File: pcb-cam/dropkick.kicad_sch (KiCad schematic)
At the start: 50 parts, among them J1 Conn_01x13, J2 3221-10-0300-00-TR, SW1 450405020524, SW2 KMR211NG_LFS, U1 SPX3819-3.3, U2 MCP73831T-2ACI/OT, U3 CAM-M8C-0, U4 ATSAMD21G18A-AUT, U5 DPS310XTSA1, U6 MPU-6050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

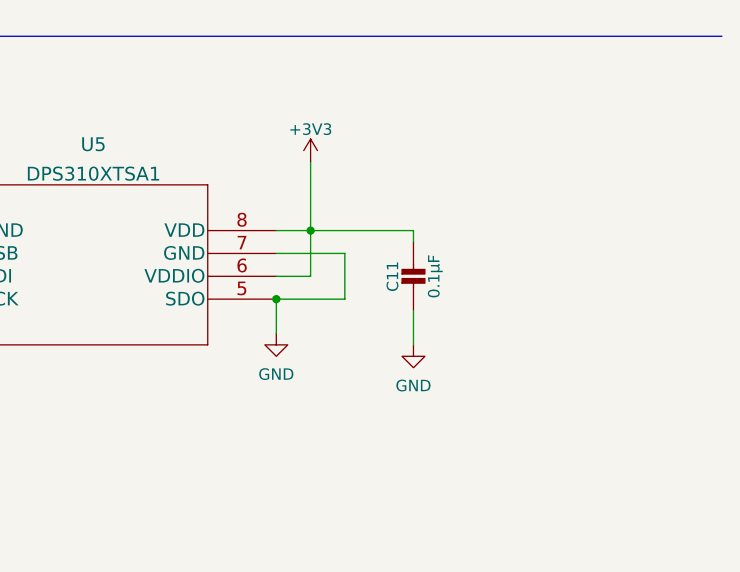
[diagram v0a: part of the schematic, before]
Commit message: Added extra CAP per DPS310 datasheet
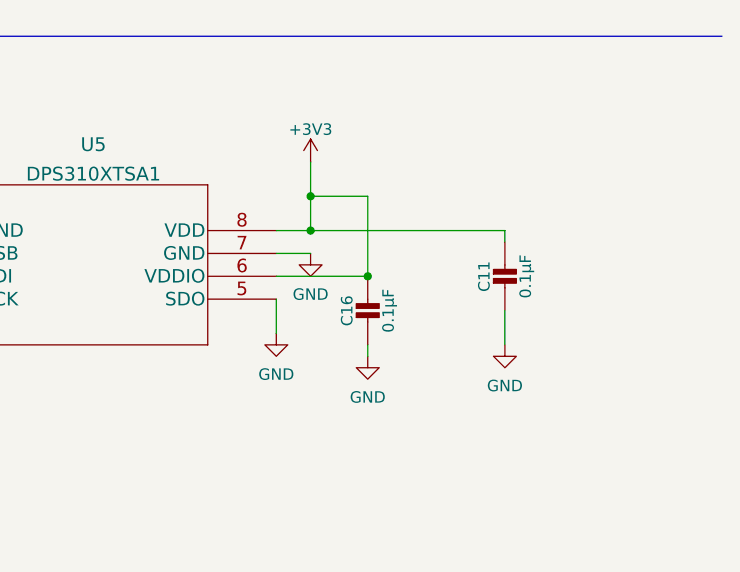
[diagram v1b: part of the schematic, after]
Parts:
- added C16: 0.1µF, Capacitor_SMD:C_0603_1608Metric, symbol Adafruit MPU6050-eagle-import:CAP_CERAMIC0603_NO
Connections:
- net +3V3: now also C16.1
- net GND: now also C16.2
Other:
- moved on the sheet: C11
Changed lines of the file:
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@@
   (junction (at 283.21 83.82) (diameter 0) (color 0 0 0 0)
   )
+  (junction (at 377.19 212.09) (diameter 0) (color 0 0 0 0)
+  )
   (junction (at 349.25 124.46) (diameter 0) (color 0 0 0 0)
   )
@@
   (junction (at 349.25 154.94) (diameter 0) (color 0 0 0 0)
   )
-  (junction (at 367.03 214.63) (diameter 0) (color 0 0 0 0)
-  )
   (junction (at 278.13 93.98) (diameter 0) (color 0 0 0 0)
   )
@@
   (junction (at 276.86 44.45) (diameter 0) (color 0 0 0 0)
   )
+  (junction (at 370.84 203.2) (diameter 0) (color 0 0 0 0)
+  )
   (junction (at 143.51 46.99) (diameter 0) (color 0 0 0 0)
   )
@@
     (stroke (width 0) (type default))
   )
-  (wire (pts (xy 370.84 207.01) (xy 382.27 207.01))
+  (wire (pts (xy 370.84 207.01) (xy 392.43 207.01))
     (stroke (width 0) (type default))
   )
@@
     (stroke (width 0) (type default))
   )
+  (wire (pts (xy 370.84 203.2) (xy 370.84 207.01))
+    (stroke (width 0) (type default))
+  )
   (wire (pts (xy 180.34 146.05) (xy 180.34 133.35))
     (stroke (width 0) (type default))
@@
     (stroke (width 0) (type default))
   )
-  (wire (pts (xy 382.27 215.9) (xy 382.27 219.71))
+  (wire (pts (xy 392.43 215.9) (xy 392.43 219.71))
     (stroke (width 0) (type default))
   )
@@
     (stroke (width 0) (type default))
   )
-  (wire (pts (xy 370.84 212.09) (xy 367.03 212.09))
-    (stroke (width 0) (type default))
-  )
   (wire (pts (xy 349.25 121.92) (xy 349.25 124.46))
     (stroke (width 0) (type default))
@@
     (stroke (width 0) (type default))
   )
-  (wire (pts (xy 382.27 207.01) (xy 382.27 208.28))
+  (wire (pts (xy 392.43 207.01) (xy 392.43 208.28))
     (stroke (width 0) (type default))
   )
@@
     (stroke (width 0) (type default))
   )
+  (wire (pts (xy 367.03 209.55) (xy 370.84 209.55))
+    (stroke (width 0) (type default))
+  )
   (wire (pts (xy 27.94 39.37) (xy 22.86 39.37))
     (stroke (width 0) (type default))
@@
     (stroke (width 0) (type default))
   )
-  (wire (pts (xy 374.65 214.63) (xy 367.03 214.63))
-    (stroke (width 0) (type default))
-  )
   (wire (pts (xy 100.33 52.07) (xy 100.33 57.15))
     (stroke (width 0) (type default))
@@
     (stroke (width 0) (type default))
   )
+  (wire (pts (xy 367.03 212.09) (xy 377.19 212.09))
+    (stroke (width 0) (type default))
+  )
   (wire (pts (xy 58.42 54.61) (xy 58.42 57.15))
     (stroke (width 0) (type default))
@@
     (stroke (width 0) (type default))
   )
-  (wire (pts (xy 374.65 209.55) (xy 374.65 214.63))
+  (wire (pts (xy 250.19 38.1) (xy 250.19 35.56))
     (stroke (width 0) (type default))
   )
-  (wire (pts (xy 250.19 38.1) (xy 250.19 35.56))
+  (wire (pts (xy 377.19 203.2) (xy 370.84 203.2))
     (stroke (width 0) (type default))
   )
@@
     (stroke (width 0) (type default))
   )
-  (wire (pts (xy 367.03 209.55) (xy 374.65 209.55))
+  (wire (pts (xy 377.19 219.71) (xy 377.19 220.98))
     (stroke (width 0) (type default))
   )
@@
     (stroke (width 0) (type default))
   )
+  (wire (pts (xy 377.19 212.09) (xy 377.19 203.2))
+    (stroke (width 0) (type default))
+  )
   (wire (pts (xy 78.74 212.09) (xy 78.74 214.63))
     (stroke (width 0) (type default))
@@
     (stroke (width 0) (type default))
   )
-  (wire (pts (xy 370.84 207.01) (xy 370.84 212.09))
-    (stroke (width 0) (type default))
-  )
   (wire (pts (xy 163.83 73.66) (xy 163.83 76.2))
     (stroke (width 0) (type default))
@@
     (stroke (width 0) (type default))
   )
-  (wire (pts (xy 370.84 199.39) (xy 370.84 207.01))
+  (wire (pts (xy 370.84 199.39) (xy 370.84 203.2))
     (stroke (width 0) (type default))
   )
@@
     )
   )
+  (symbol (lib_id "power:GND") (at 370.84 209.55 0) (unit 1)
+    (in_bom yes) (on_board yes) (dnp no) (fields_autoplaced)
+    (property "Reference" "#PWR08" (at 370.84 215.9 0)
+      (effects (font (size 1.27 1.27)) hide)
+    )
+    (property "Value" "GND" (at 370.84 214.1125 0)
+      (effects (font (size 1.27 1.27)))
+    )
+    (property "Footprint" "" (at 370.84 209.55 0)
+      (effects (font (size 1.27 1.27)) hide)
+    )
+    (property "Datasheet" "" (at 370.84 209.55 0)
+      (effects (font (size 1.27 1.27)) hide)
+    )
+    (pin "1")
+    (instances
+      (project "dropkick"
+        (path "/2b2dde1b-cbce-41fa-8b99-d2f668db6852"
+          (reference "#PWR08") (unit 1)
+        )
+      )
+    )
+  )
   (symbol (lib_id "Adafruit Feather M0 Adalogger-eagle-import:GND") (at 129.54 76.2 180) (unit 1)
     (in_bom yes) (on_board yes) (dnp no)
@@
     )
   )
+  (symbol (lib_id "power:GND") (at 377.19 220.98 0) (unit 1)
+    (in_bom yes) (on_board yes) (dnp no) (fields_autoplaced)
+    (property "Reference" "#PWR09" (at 377.19 227.33 0)
+      (effects (font (size 1.27 1.27)) hide)
+    )
+    (property "Value" "GND" (at 377.19 225.5425 0)
+      (effects (font (size 1.27 1.27)))
+    )
+    (property "Footprint" "" (at 377.19 220.98 0)
+      (effects (font (size 1.27 1.27)) hide)
+    )
+    (property "Datasheet" "" (at 377.19 220.98 0)
+      (effects (font (size 1.27 1.27)) hide)
+    )
+    (pin "1")
+    (instances
+      (project "dropkick"
+        (path "/2b2dde1b-cbce-41fa-8b99-d2f668db6852"
+          (reference "#PWR09") (unit 1)
+        )
+      )
+    )
+  )
   (symbol (lib_id "Adafruit MPU6050-eagle-import:GND") (at 31.75 234.95 0) (unit 1)
     (in_bom yes) (on_board yes) (dnp no)
@@
     )
   )
-  (symbol (lib_id "Adafruit MPU6050-eagle-import:CAP_CERAMIC0603_NO") (at 382.27 213.36 0) (unit 1)
+  (symbol (lib_id "Adafruit MPU6050-eagle-import:CAP_CERAMIC0603_NO") (at 392.43 213.36 0) (unit 1)
     (in_bom yes) (on_board yes) (dnp no)
-    (property "Reference" "C11" (at 379.98 212.11 90)
+    (property "Reference" "C11" (at 390.14 212.11 90)
       (effects (font (size 1.27 1.27)))
     )
-    (property "Value" "0.1µF" (at 384.57 212.11 90)
+    (property "Value" "0.1µF" (at 394.73 212.11 90)
       (effects (font (size 1.27 1.27)))
     )
-    (property "Footprint" "Capacitor_SMD:C_0603_1608Metric" (at 382.27 213.36 0)
+    (property "Footprint" "Capacitor_SMD:C_0603_1608Metric" (at 392.43 213.36 0)
       (effects (font (size 1.27 1.27)) hide)
     )
-    (property "Datasheet" "" (at 382.27 213.36 0)
+    (property "Datasheet" "" (at 392.43 213.36 0)
       (effects (font (size 1.27 1.27)) hide)
     )
-    (property "Manufacturer Part" "VJ0603Y104JXXAC" (at 382.27 213.36 0)
+    (property "Manufacturer Part" "VJ0603Y104JXXAC" (at 392.43 213.36 0)
       (effects (font (size 1.27 1.27)) hide)
     )
@@
     )
   )
+  (symbol (lib_id "Adafruit MPU6050-eagle-import:CAP_CERAMIC0603_NO") (at 377.19 217.17 0) (unit 1)
+    (in_bom yes) (on_board yes) (dnp no)
+    (property "Reference" "C16" (at 374.9 215.92 90)
+      (effects (font (size 1.27 1.27)))
+    )
+    (property "Value" "0.1µF" (at 379.49 215.92 90)
+      (effects (font (size 1.27 1.27)))
+    )
+    (property "Footprint" "Capacitor_SMD:C_0603_1608Metric" (at 377.19 217.17 0)
+      (effects (font (size 1.27 1.27)) hide)
+    )
+    (property "Datasheet" "" (at 377.19 217.17 0)
+      (effects (font (size 1.27 1.27)) hide)
+    )
+    (property "Manufacturer Part" "VJ0603Y104JXXAC" (at 377.19 217.17 0)
+      (effects (font (size 1.27 1.27)) hide)
+    )
+    (pin "1")
+    (pin "2")
+    (instances
+      (project "dropkick"
+        (path "/2b2dde1b-cbce-41fa-8b99-d2f668db6852"
+          (reference "C16") (unit 1)
+        )
+      )
+    )
+  )
   (symbol (lib_id "power:+3V3") (at 370.84 199.39 0) (unit 1)
     (in_bom yes) (on_board yes) (dnp no) (fields_autoplaced)
@@
     )
   )
-  (symbol (lib_id "power:GND") (at 382.27 219.71 0) (unit 1)
+  (symbol (lib_id "power:GND") (at 392.43 219.71 0) (unit 1)
     (in_bom yes) (on_board yes) (dnp no) (fields_autoplaced)
-    (property "Reference" "#PWR012" (at 382.27 226.06 0)
+    (property "Reference" "#PWR012" (at 392.43 226.06 0)
       (effects (font (size 1.27 1.27)) hide)
     )
-    (property "Value" "GND" (at 382.27 224.2725 0)
+    (property "Value" "GND" (at 392.43 224.2725 0)
       (effects (font (size 1.27 1.27)))
     )
-    (property "Footprint" "" (at 382.27 219.71 0)
+    (property "Footprint" "" (at 392.43 219.71 0)
       (effects (font (size 1.27 1.27)) hide)
     )
-    (property "Datasheet" "" (at 382.27 219.71 0)
+    (property "Datasheet" "" (at 392.43 219.71 0)
       (effects (font (size 1.27 1.27)) hide)
     )

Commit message: Add boxes to schematic; clean up PCB placement; use PCBWay gerber settings
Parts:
- CHG1: value ORANGE LED -> ORANGE
- L1, L3: value GREEN LED -> GREEN
- L2: value RED LED -> RED
- U4: value ATSAMD21G18A-AUT -> ATSAMD21G18A-AU; Manufacturer Part ATSAMD21G18A-AUT -> ATSAMD21G18A-AU
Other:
- note added: "+3.3V 500mA POWER AND FILTERING"
- note added: "2.0mm pitch pads"
- note added: "BAROMETRIC SENSOR - I2C"
- note added: "Charge Current - R4"
- note added: "GNSS RECEIVER AND BATTERY BACKUP - CAM-M8C"
- note added: "INERTIAL SENSOR - I2C"
- note added: "PROGRAMMABLE LEDS"
- note removed: "2mm pitch pads"
- note removed: "GNSS RECEIVER - CAM-M8C"
- note removed: "Inertial / Air Pressure Sensors"
- note removed: "LEDS"
- note removed: "POWER AND FILTERING"
- moved on the sheet: B1, C12, C13, C14, C15, C6, R6, R7, U3, U6

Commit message: Update switch
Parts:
- SW2: footprint lib_fp:KMR211NG LFS -> logger:KMR211NG LFS
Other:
- moved on the sheet: SW2
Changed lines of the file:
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@@
   (junction (at 180.34 215.9) (diameter 0) (color 0 0 0 0)
   )
+  (junction (at 142.24 45.72) (diameter 0) (color 0 0 0 0)
+  )
   (junction (at 163.83 73.66) (diameter 0) (color 0 0 0 0)
   )
@@
   (junction (at 323.85 109.22) (diameter 0) (color 0 0 0 0)
   )
+  (junction (at 118.11 34.29) (diameter 0) (color 0 0 0 0)
+  )
   (junction (at 313.69 209.55) (diameter 0) (color 0 0 0 0)
   )
@@
   (junction (at 370.84 203.2) (diameter 0) (color 0 0 0 0)
   )
-  (junction (at 143.51 53.34) (diameter 0) (color 0 0 0 0)
-  )
   (junction (at 22.86 39.37) (diameter 0) (color 0 0 0 0)
   )
@@
   (junction (at 27.94 39.37) (diameter 0) (color 0 0 0 0)
   )
-  (junction (at 143.51 29.21) (diameter 0) (color 0 0 0 0)
-  )
   (junction (at 78.74 212.09) (diameter 0) (color 0 0 0 0)
   )
@@
     (stroke (width 0) (type default))
   )
-  (wire (pts (xy 143.51 29.21) (xy 143.51 35.56))
-    (stroke (width 0) (type default))
-  )
   (wire (pts (xy 248.92 231.14) (xy 264.16 231.14))
     (stroke (width 0) (type default))
@@
     (stroke (width 0) (type default))
   )
-  (wire (pts (xy 143.51 53.34) (xy 118.11 53.34))
-    (stroke (width 0) (type default))
-  )
   (wire (pts (xy 35.56 44.45) (xy 35.56 57.15))
     (stroke (width 0) (type default))
@@
     (stroke (width 0) (type default))
   )
-  (wire (pts (xy 143.51 44.45) (xy 143.51 53.34))
-    (stroke (width 0) (type default))
-  )
   (wire (pts (xy 185.42 158.75) (xy 185.42 161.29))
     (stroke (width 0) (type default))
@@
     (stroke (width 0) (type default))
   )
-  (wire (pts (xy 143.51 53.34) (xy 143.51 57.15))
-    (stroke (width 0) (type default))
-  )
   (wire (pts (xy 92.71 33.02) (xy 92.71 38.1))
     (stroke (width 0) (type default))
@@
     (stroke (width 0) (type default))
   )
-  (wire (pts (xy 143.51 25.4) (xy 143.51 29.21))
-    (stroke (width 0) (type default))
-  )
   (wire (pts (xy 38.1 111.76) (xy 33.02 111.76))
     (stroke (width 0) (type default))
@@
     (stroke (width 0) (type default))
   )
-  (wire (pts (xy 135.89 25.4) (xy 143.51 25.4))
-    (stroke (width 0) (type default))
-  )
   (wire (pts (xy 119.38 86.36) (xy 119.38 91.44))
     (stroke (width 0) (type default))
@@
     (stroke (width 0) (type default))
   )
-  (wire (pts (xy 118.11 53.34) (xy 118.11 44.45))
-    (stroke (width 0) (type default))
-  )
   (wire (pts (xy 127 214.63) (xy 138.43 214.63))
     (stroke (width 0) (type default))
@@
     (stroke (width 0) (type default))
   )
-  (wire (pts (xy 143.51 29.21) (xy 118.11 29.21))
-    (stroke (width 0) (type default))
-  )
   (wire (pts (xy 107.95 57.15) (xy 107.95 52.07))
     (stroke (width 0) (type default))
@@
     (stroke (width 0) (type default))
   )
+  (wire (pts (xy 118.11 29.21) (xy 118.11 34.29))
+    (stroke (width 0) (type default))
+  )
   (wire (pts (xy 304.8 77.47) (xy 309.88 77.47))
     (stroke (width 0) (type default))
@@
     (stroke (width 0) (type default))
   )
+  (wire (pts (xy 142.24 45.72) (xy 142.24 50.8))
+    (stroke (width 0) (type default))
+  )
   (wire (pts (xy 180.34 156.21) (xy 180.34 161.29))
     (stroke (width 0) (type default))
@@
     (stroke (width 0) (type default))
   )
-  (wire (pts (xy 118.11 29.21) (xy 118.11 35.56))
-    (stroke (width 0) (type default))
-  )
   (wire (pts (xy 227.33 71.12) (xy 227.33 73.66))
     (stroke (width 0) (type default))
@@
     (stroke (width 0) (type default))
   )
+  (wire (pts (xy 142.24 34.29) (xy 142.24 45.72))
+    (stroke (width 0) (type default))
+  )
   (wire (pts (xy 33.02 104.14) (xy 33.02 101.6))
     (stroke (width 0) (type default))
@@
     (stroke (width 0) (type default))
   )
+  (wire (pts (xy 118.11 34.29) (xy 118.11 45.72))
+    (stroke (width 0) (type default))
+  )
   (rectangle (start 214.63 13.97) (end 297.18 102.87)
     (stroke (width 0) (type default))
@@
     (effects (font (size 1.2446 1.2446)) (justify left bottom))
   )
-  (label "~{RESET}" (at 135.89 25.4 0) (fields_autoplaced)
+  (label "~{RESET}" (at 118.11 29.21 0) (fields_autoplaced)
     (effects (font (size 1.2446 1.2446)) (justify left bottom))
   )
@@
     )
   )
-  (symbol (lib_id "Adafruit Feather M0 Adalogger-eagle-import:GND") (at 143.51 59.69 0) (unit 1)
+  (symbol (lib_id "Adafruit Feather M0 Adalogger-eagle-import:GND") (at 142.24 53.34 0) (unit 1)
     (in_bom yes) (on_board yes) (dnp no)
-    (property "Reference" "#GND01" (at 143.51 59.69 0)
+    (property "Reference" "#GND01" (at 142.24 53.34 0)
       (effects (font (size 1.27 1.27)) hide)
     )
-    (property "Value" "GND" (at 140.97 62.23 0)
+    (property "Value" "GND" (at 139.7 55.88 0)
       (effects (font (size 1.778 1.5113)) (justify left bottom))
     )
-    (property "Footprint" "" (at 143.51 59.69 0)
+    (property "Footprint" "" (at 142.24 53.34 0)
       (effects (font (size 1.27 1.27)) hide)
     )
-    (property "Datasheet" "" (at 143.51 59.69 0)
+    (property "Datasheet" "" (at 142.24 53.34 0)
       (effects (font (size 1.27 1.27)) hide)
     )
@@
   (symbol (lib_id "dropkick:KMR211NG_LFS") (at 130.81 39.37 0) (unit 1)
     (in_bom yes) (on_board yes) (dnp no)
-    (property "Reference" "SW2" (at 130.81 33.02 0)
+    (property "Reference" "SW2" (at 130.81 30.48 0)
       (effects (font (size 1.524 1.524)))
     )
@@
       (effects (font (size 1.524 1.524)) hide)
     )
-    (property "Footprint" "lib_fp:KMR211NG LFS" (at 129.54 28.194 0)
+    (property "Footprint" "logger:KMR211NG LFS" (at 129.54 28.194 0)
       (effects (font (size 1.524 1.524)) hide)
     )
